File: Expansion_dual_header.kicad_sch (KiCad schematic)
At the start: 6 parts, among them J3 ESQ-120-14-G-S, J4 ESQ-120-14-G-S, J5 Conn_01x02_Pin, J6 Conn_01x02_Pin

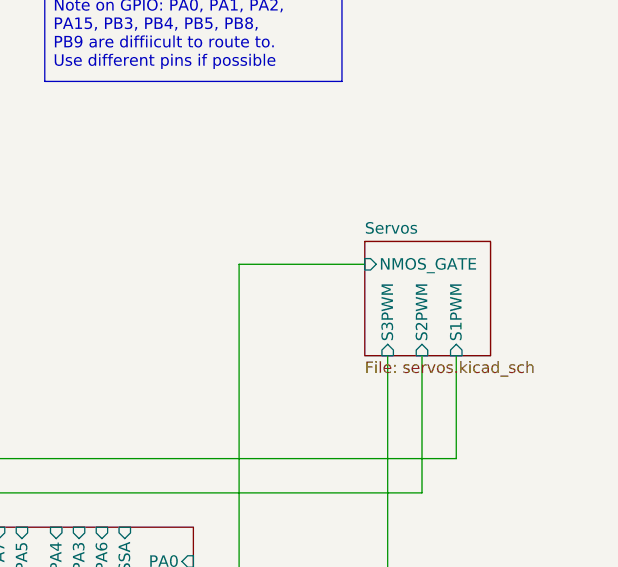
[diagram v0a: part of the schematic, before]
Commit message: updated servos page with em connections
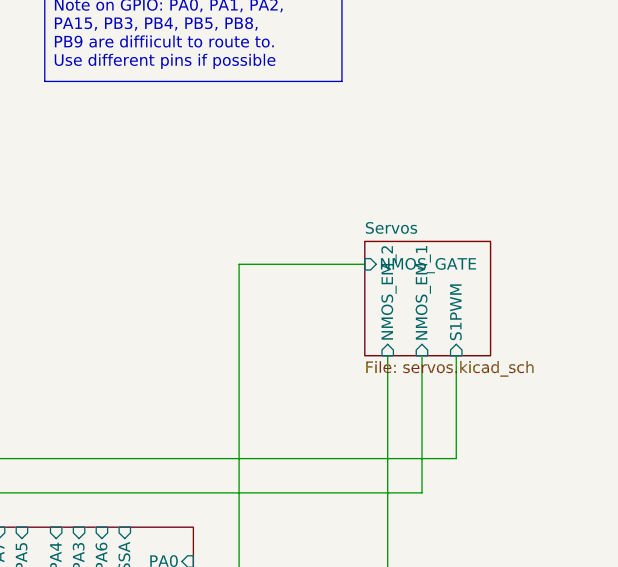
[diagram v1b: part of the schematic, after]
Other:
- sheet Servos ports: added NMOS_EM_1, NMOS_EM_2; removed S2PWM, S3PWM
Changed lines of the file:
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@@
 			)
 		)
-		(pin "S2PWM" input
-			(at 270.51 57.15 270)
+		(pin "NMOS_GATE" input
+			(at 264.16 46.99 180)
 			(effects
 				(font
@@
 			)
 		)
-		(pin "S3PWM" input
+		(pin "NMOS_EM_2" input
 			(at 266.7 57.15 270)
 			(effects
@@
 			)
 		)
-		(pin "NMOS_GATE" input
-			(at 264.16 46.99 180)
+		(pin "NMOS_EM_1" input
+			(at 270.51 57.15 270)
 			(effects
 				(font
